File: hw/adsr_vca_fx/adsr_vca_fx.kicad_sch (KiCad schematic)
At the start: 0 parts

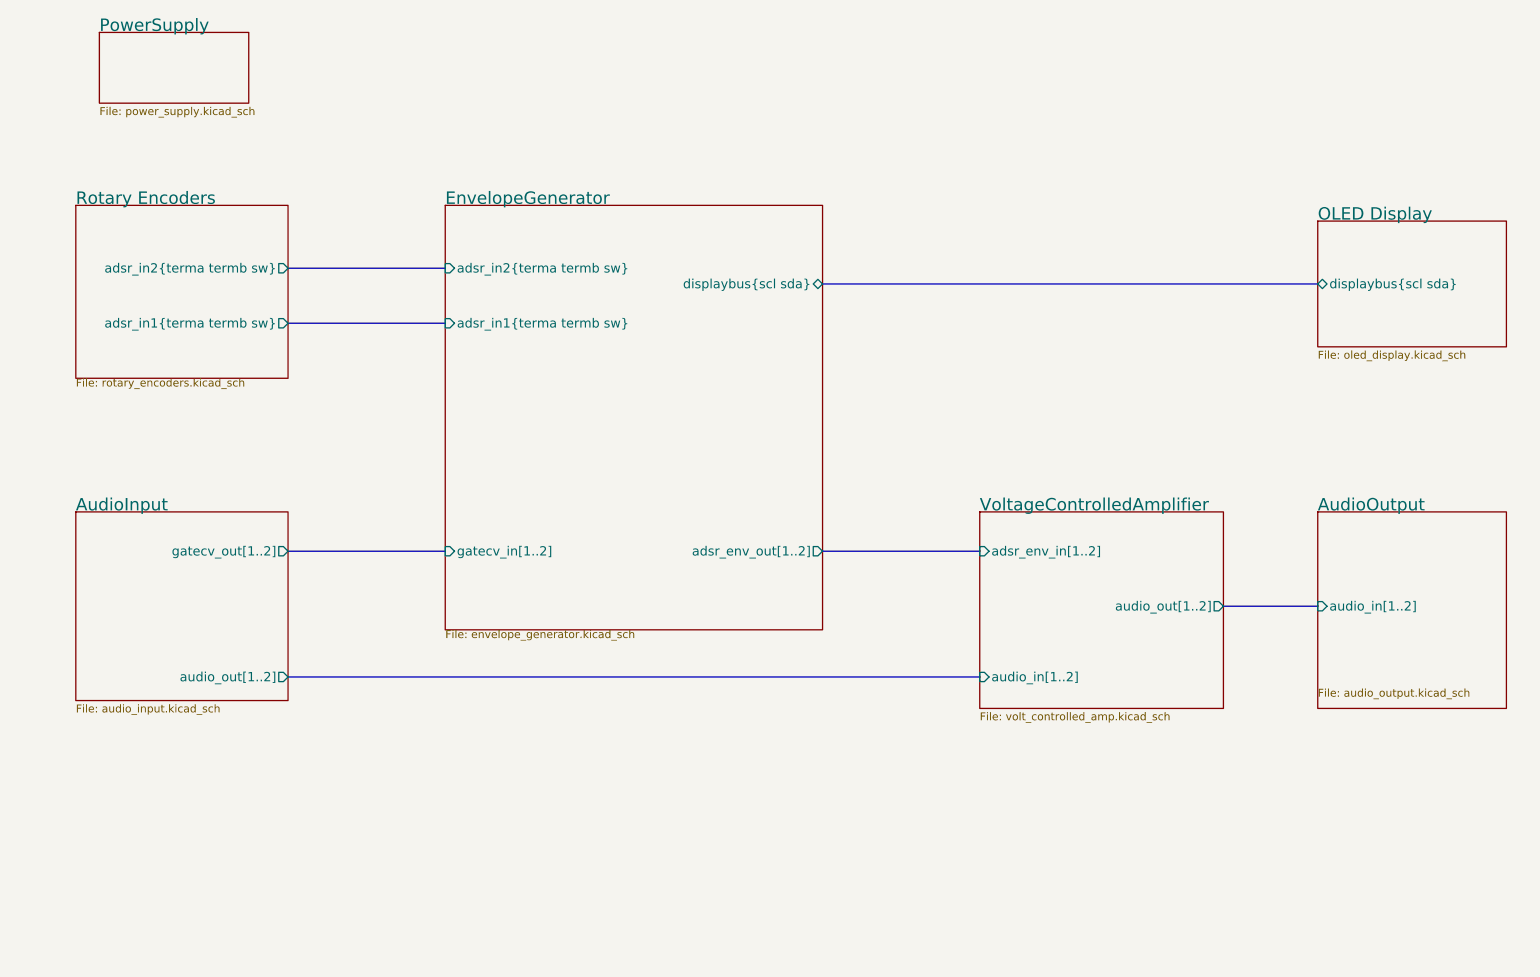
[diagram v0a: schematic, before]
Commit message: modified design into normal/inverted envlope
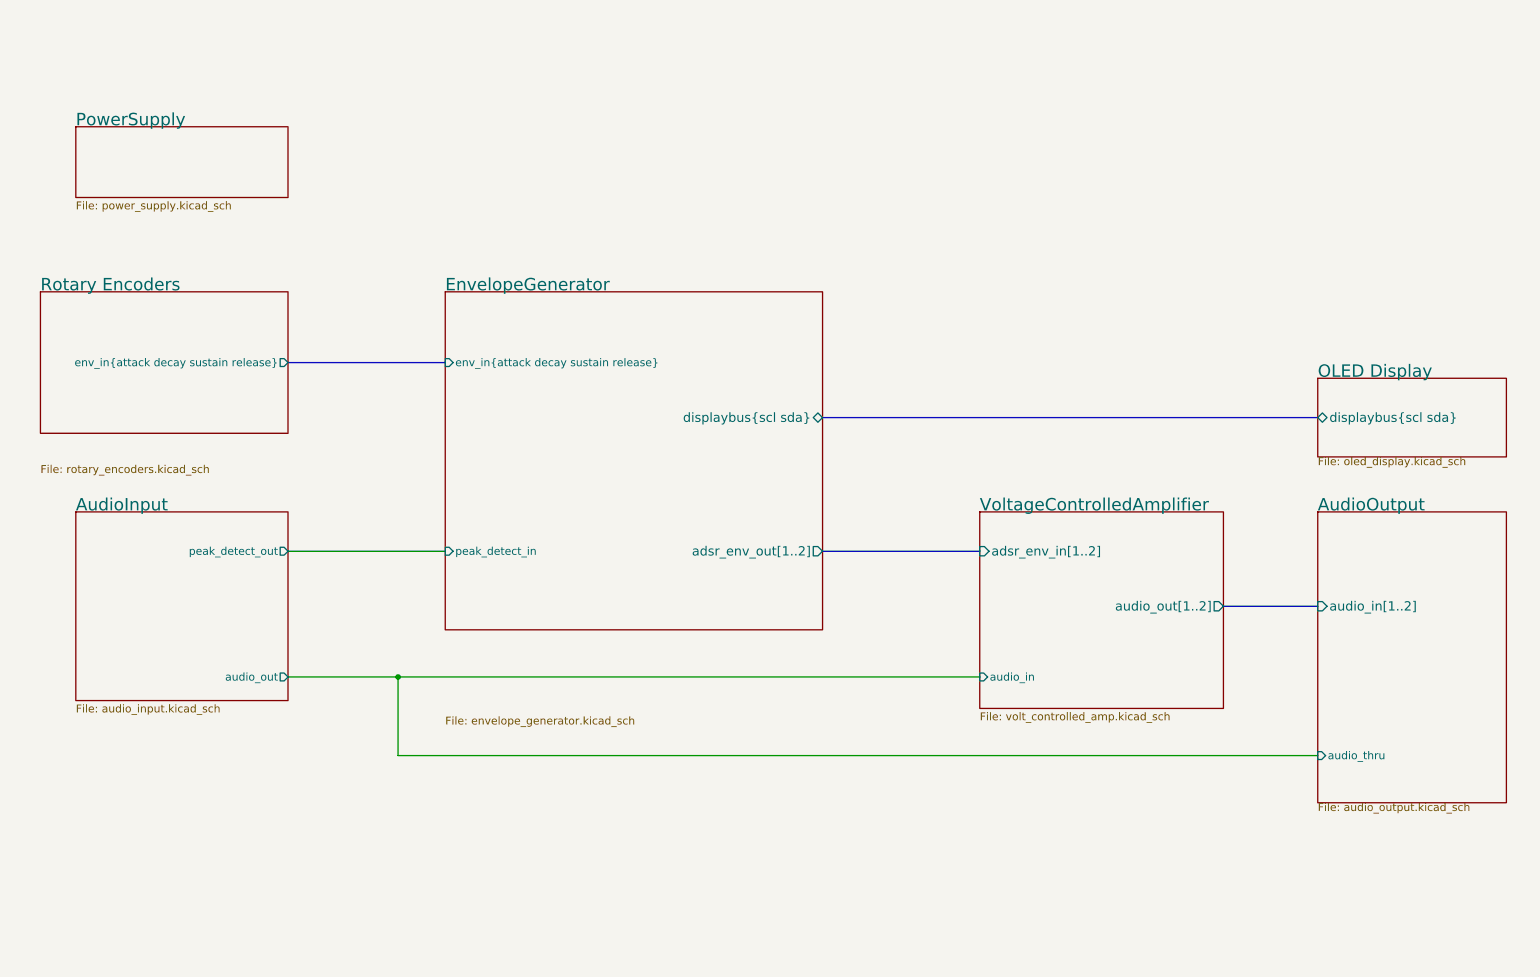
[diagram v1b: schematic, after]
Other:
- sheet AudioInput ports: added audio_out, peak_detect_out; removed audio_out[1..2], gatecv_out[1..2]
- sheet AudioOutput ports: added audio_thru; removed none
- sheet EnvelopeGenerator ports: added env_in{attack decay sustain release}, peak_detect_in; removed adsr_in1{terma termb sw}, adsr_in2{terma termb sw}, gatecv_in[1..2]
- sheet Rotary Encoders ports: added env_in{attack decay sustain release}; removed adsr_in1{terma termb sw}, adsr_in2{terma termb sw}
- sheet VoltageControlledAmplifier ports: added audio_in; removed audio_in[1..2]
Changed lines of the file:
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@@
 (kicad_sch (version 20230121) (generator eeschema)
   (paper "A4")
+  (junction (at 81.28 133.35) (diameter 0) (color 0 0 0 0)
+  )
   (bus (pts (xy 214.63 121.92) (xy 229.87 121.92))
+    (stroke (width 0) (type default))
+  )
+  (wire (pts (xy 81.28 133.35) (xy 63.5 133.35))
     (stroke (width 0) (type default))
   )
@@
     (stroke (width 0) (type default))
   )
-  (bus (pts (xy 63.5 76.2) (xy 88.9 76.2))
+  (bus (pts (xy 63.5 82.55) (xy 88.9 82.55))
     (stroke (width 0) (type default))
   )
-  (bus (pts (xy 63.5 67.31) (xy 88.9 67.31))
+  (wire (pts (xy 229.87 146.05) (xy 81.28 146.05))
     (stroke (width 0) (type default))
   )
-  (bus (pts (xy 63.5 113.03) (xy 88.9 113.03))
+  (wire (pts (xy 81.28 146.05) (xy 81.28 133.35))
     (stroke (width 0) (type default))
   )
-  (bus (pts (xy 63.5 133.35) (xy 175.26 133.35))
+  (wire (pts (xy 63.5 113.03) (xy 88.9 113.03))
     (stroke (width 0) (type default))
   )
-  (bus (pts (xy 149.86 69.85) (xy 229.87 69.85))
+  (wire (pts (xy 81.28 133.35) (xy 175.26 133.35))
+    (stroke (width 0) (type default))
+  )
+  (bus (pts (xy 149.86 91.44) (xy 229.87 91.44))
     (stroke (width 0) (type default))
   )
@@
       (effects (font (size 1.5 1.5)) (justify right))
     )
-    (pin "audio_in[1..2]" input (at 175.26 133.35 180)
+    (pin "adsr_env_in[1..2]" input (at 175.26 113.03 180)
       (effects (font (size 1.5 1.5)) (justify left))
     )
-    (pin "adsr_env_in[1..2]" input (at 175.26 113.03 180)
-      (effects (font (size 1.5 1.5)) (justify left))
+    (pin "audio_in" input (at 175.26 133.35 180)
+      (effects (font (size 1.27 1.27)) (justify left))
     )
     (instances
@@
       (effects (font (size 1.27 1.27)) (justify left top))
     )
-    (pin "audio_out[1..2]" output (at 63.5 133.35 0)
-      (effects (font (size 1.5 1.5)) (justify right))
+    (pin "audio_out" output (at 63.5 133.35 0)
+      (effects (font (size 1.27 1.27)) (justify right))
     )
-    (pin "gatecv_out[1..2]" output (at 63.5 113.03 0)
-      (effects (font (size 1.5 1.5)) (justify right))
+    (pin "peak_detect_out" output (at 63.5 113.03 0)
+      (effects (font (size 1.27 1.27)) (justify right))
     )
     (instances
@@
     )
   )
-  (sheet (at 229.87 59.69) (size 30.48 20.32)
+  (sheet (at 229.87 85.09) (size 30.48 12.7)
     (stroke (width 0.1524) (type solid))
     (fill (color 0 0 0 0.0000))
-    (property "Sheetname" "OLED Display" (at 229.87 59.69 0)
+    (property "Sheetname" "OLED Display" (at 229.87 85.09 0)
       (effects (font (size 2 2)) (justify left bottom))
     )
-    (property "Sheetfile" "oled_display.kicad_sch" (at 229.87 80.5946 0)
+    (property "Sheetfile" "oled_display.kicad_sch" (at 229.87 97.79 0)
       (effects (font (size 1.27 1.27)) (justify left top))
     )
-    (property "Field2" "" (at 229.87 59.69 0)
+    (property "Field2" "" (at 229.87 85.09 0)
       (effects (font (size 1.27 1.27)) hide)
     )
-    (pin "displaybus{scl sda}" bidirectional (at 229.87 69.85 180)
+    (pin "displaybus{scl sda}" bidirectional (at 229.87 91.44 180)
       (effects (font (size 1.5 1.5)) (justify left))
     )
@@
     )
   )
-  (sheet (at 88.9 57.15) (size 60.96 68.58)
+  (sheet (at 88.9 71.12) (size 60.96 54.61)
     (stroke (width 0.1524) (type solid))
     (fill (color 0 0 0 0.0000))
-    (property "Sheetname" "EnvelopeGenerator" (at 88.9 57.15 0)
+    (property "Sheetname" "EnvelopeGenerator" (at 88.9 71.12 0)
       (effects (font (size 2 2)) (justify left bottom))
     )
-    (property "Sheetfile" "envelope_generator.kicad_sch" (at 88.9 125.73 0)
+    (property "Sheetfile" "envelope_generator.kicad_sch" (at 88.9 139.7 0)
       (effects (font (size 1.27 1.27)) (justify left top))
     )
-    (pin "displaybus{scl sda}" bidirectional (at 149.86 69.85 0)
+    (pin "displaybus{scl sda}" bidirectional (at 149.86 91.44 0)
       (effects (font (size 1.5 1.5)) (justify right))
-    )
-    (pin "adsr_in2{terma termb sw}" input (at 88.9 67.31 180)
-      (effects (font (size 1.5 1.5)) (justify left))
-    )
-    (pin "adsr_in1{terma termb sw}" input (at 88.9 76.2 180)
-      (effects (font (size 1.5 1.5)) (justify left))
-    )
-    (pin "gatecv_in[1..2]" input (at 88.9 113.03 180)
-      (effects (font (size 1.5 1.5)) (justify left))
     )
     (pin "adsr_env_out[1..2]" output (at 149.86 113.03 0)
       (effects (font (size 1.5 1.5)) (justify right))
+    )
+    (pin "peak_detect_in" input (at 88.9 113.03 180)
+      (effects (font (size 1.27 1.27)) (justify left))
+    )
+    (pin "env_in{attack decay sustain release}" input (at 88.9 82.55 180)
+      (effects (font (size 1.27 1.27)) (justify left))
     )
     (instances
@@
     )
   )
-  (sheet (at 29.21 57.15) (size 34.29 27.94)
+  (sheet (at 23.495 71.12) (size 40.005 22.86)
     (stroke (width 0.1524) (type solid))
     (fill (color 0 0 0 0.0000))
-    (property "Sheetname" "Rotary Encoders" (at 29.21 57.15 0)
+    (property "Sheetname" "Rotary Encoders" (at 23.495 71.12 0)
       (effects (font (size 2 2)) (justify left bottom))
     )
-    (property "Sheetfile" "rotary_encoders.kicad_sch" (at 29.21 85.09 0)
+    (property "Sheetfile" "rotary_encoders.kicad_sch" (at 23.495 99.06 0)
       (effects (font (size 1.27 1.27)) (justify left top))
     )
-    (property "Field2" "" (at 29.21 57.15 0)
+    (property "Field2" "" (at 23.495 71.12 0)
       (effects (font (size 1.27 1.27)) hide)
     )
-    (pin "adsr_in2{terma termb sw}" output (at 63.5 67.31 0)
-      (effects (font (size 1.5 1.5)) (justify right))
-    )
-    (pin "adsr_in1{terma termb sw}" output (at 63.5 76.2 0)
-      (effects (font (size 1.5 1.5)) (justify right))
+    (pin "env_in{attack decay sustain release}" output (at 63.5 82.55 0)
+      (effects (font (size 1.27 1.27)) (justify right))
     )
     (instances
@@
     )
   )
-  (sheet (at 229.87 106.68) (size 30.48 31.75)
+  (sheet (at 229.87 106.68) (size 30.48 46.99)
     (stroke (width 0.1524) (type solid))
     (fill (color 0 0 0 0.0000))
@@
       (effects (font (size 2 2)) (justify left bottom))
     )
-    (property "Sheetfile" "audio_output.kicad_sch" (at 229.87 135.2046 0)
+    (property "Sheetfile" "audio_output.kicad_sch" (at 229.87 153.67 0)
       (effects (font (size 1.27 1.27)) (justify left top))
     )
     (pin "audio_in[1..2]" input (at 229.87 121.92 180)
       (effects (font (size 1.5 1.5)) (justify left))
+    )
+    (pin "audio_thru" input (at 229.87 146.05 180)
+      (effects (font (size 1.27 1.27)) (justify left))
     )
     (instances
@@
     )
   )
-  (sheet (at 33.02 29.21) (size 24.13 11.43)
+  (sheet (at 29.21 44.45) (size 34.29 11.43)
     (stroke (width 0.1524) (type solid))
     (fill (color 0 0 0 0.0000))
-    (property "Sheetname" "PowerSupply" (at 33.02 29.21 0)
+    (property "Sheetname" "PowerSupply" (at 29.21 44.45 0)
       (effects (font (size 2 2)) (justify left bottom))
     )
-    (property "Sheetfile" "power_supply.kicad_sch" (at 33.02 41.2246 0)
+    (property "Sheetfile" "power_supply.kicad_sch" (at 29.21 56.4646 0)
       (effects (font (size 1.27 1.27)) (justify left top))
     )

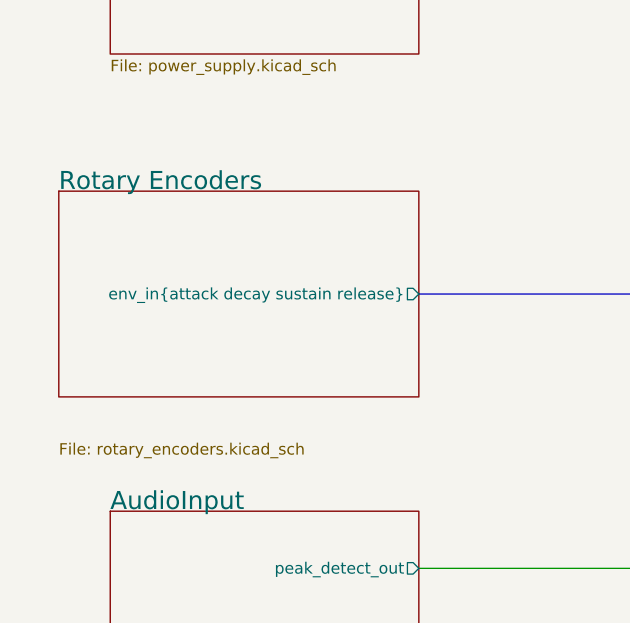
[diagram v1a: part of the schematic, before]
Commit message: renamed sheet
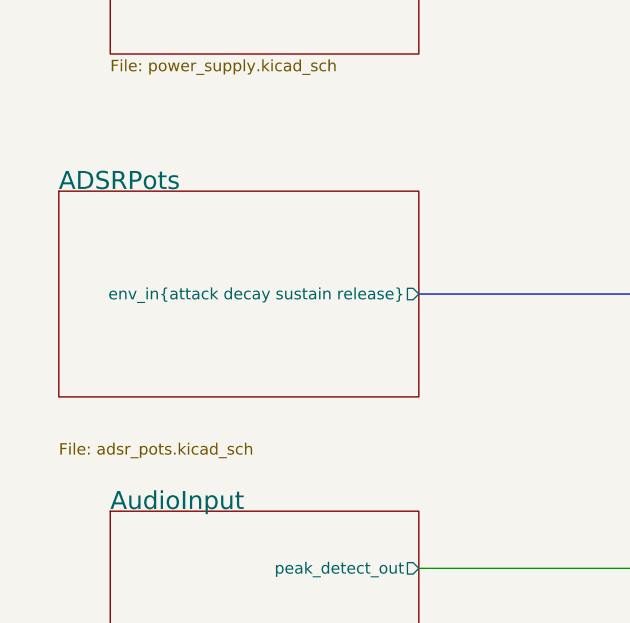
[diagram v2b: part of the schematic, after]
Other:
- sheet Rotary Encoders renamed ADSRPots
- sheet ADSRPots: file rotary_encoders.kicad_sch -> adsr_pots.kicad_sch
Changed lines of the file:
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@@
     (stroke (width 0.1524) (type solid))
     (fill (color 0 0 0 0.0000))
-    (property "Sheetname" "Rotary Encoders" (at 23.495 71.12 0)
+    (property "Sheetname" "ADSRPots" (at 23.495 71.12 0)
       (effects (font (size 2 2)) (justify left bottom))
     )
-    (property "Sheetfile" "rotary_encoders.kicad_sch" (at 23.495 99.06 0)
+    (property "Sheetfile" "adsr_pots.kicad_sch" (at 23.495 99.06 0)
       (effects (font (size 1.27 1.27)) (justify left top))
     )

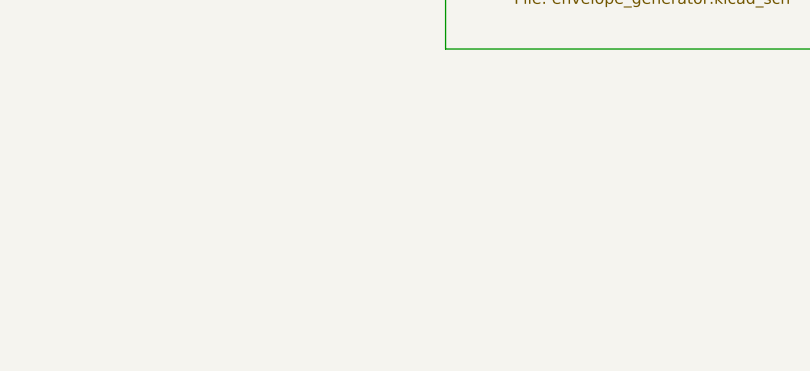
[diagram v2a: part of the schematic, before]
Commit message: updated layout
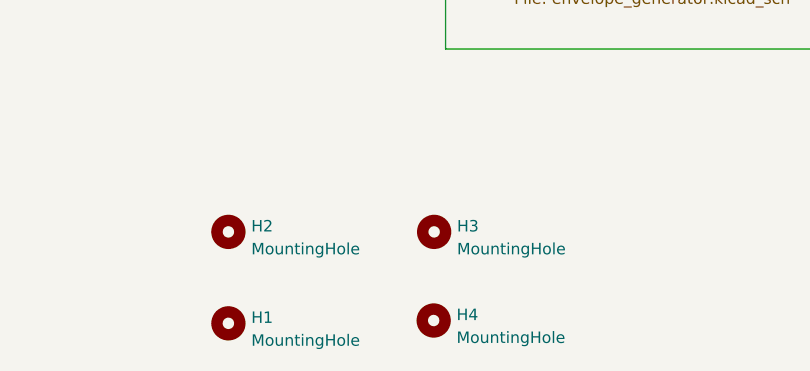
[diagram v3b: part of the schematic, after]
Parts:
- added H1, H2, H3, H4: MountingHole, MountingHole:MountingHole_3mm_Pad, symbol Mechanical:MountingHole
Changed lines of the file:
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@@
     (stroke (width 0) (type default))
+  )
+  (symbol (lib_id "Mechanical:MountingHole") (at 57.15 176.53 0) (unit 1)
+    (in_bom no) (on_board yes) (dnp no) (fields_autoplaced)
+    (property "Reference" "H1" (at 59.69 175.895 0)
+      (effects (font (size 1.27 1.27)) (justify left))
+    )
+    (property "Value" "MountingHole" (at 59.69 178.435 0)
+      (effects (font (size 1.27 1.27)) (justify left))
+    )
+    (property "Footprint" "MountingHole:MountingHole_3mm_Pad" (at 57.15 176.53 0)
+      (effects (font (size 1.27 1.27)) hide)
+    )
+    (property "Datasheet" "~" (at 57.15 176.53 0)
+      (effects (font (size 1.27 1.27)) hide)
+    )
+    (instances
+      (project "adsr_vca_fx"
+        (path "/2c7cc946-dcca-4ffb-b6a0-bf0c9ddb491b"
+          (reference "H1") (unit 1)
+        )
+      )
+    )
+  )
+  (symbol (lib_id "Mechanical:MountingHole") (at 57.15 166.37 0) (unit 1)
+    (in_bom no) (on_board yes) (dnp no) (fields_autoplaced)
+    (property "Reference" "H2" (at 59.69 165.735 0)
+      (effects (font (size 1.27 1.27)) (justify left))
+    )
+    (property "Value" "MountingHole" (at 59.69 168.275 0)
+      (effects (font (size 1.27 1.27)) (justify left))
+    )
+    (property "Footprint" "MountingHole:MountingHole_3mm_Pad" (at 57.15 166.37 0)
+      (effects (font (size 1.27 1.27)) hide)
+    )
+    (property "Datasheet" "~" (at 57.15 166.37 0)
+      (effects (font (size 1.27 1.27)) hide)
+    )
+    (instances
+      (project "adsr_vca_fx"
+        (path "/2c7cc946-dcca-4ffb-b6a0-bf0c9ddb491b"
+          (reference "H2") (unit 1)
+        )
+      )
+    )
+  )
+  (symbol (lib_id "Mechanical:MountingHole") (at 80.01 166.37 0) (unit 1)
+    (in_bom no) (on_board yes) (dnp no) (fields_autoplaced)
+    (property "Reference" "H3" (at 82.55 165.735 0)
+      (effects (font (size 1.27 1.27)) (justify left))
+    )
+    (property "Value" "MountingHole" (at 82.55 168.275 0)
+      (effects (font (size 1.27 1.27)) (justify left))
+    )
+    (property "Footprint" "MountingHole:MountingHole_3mm_Pad" (at 80.01 166.37 0)
+      (effects (font (size 1.27 1.27)) hide)
+    )
+    (property "Datasheet" "~" (at 80.01 166.37 0)
+      (effects (font (size 1.27 1.27)) hide)
+    )
+    (instances
+      (project "adsr_vca_fx"
+        (path "/2c7cc946-dcca-4ffb-b6a0-bf0c9ddb491b"
+          (reference "H3") (unit 1)
+        )
+      )
+    )
+  )
+  (symbol (lib_id "Mechanical:MountingHole") (at 79.9585 176.2167 0) (unit 1)
+    (in_bom no) (on_board yes) (dnp no) (fields_autoplaced)
+    (property "Reference" "H4" (at 82.4985 175.5817 0)
+      (effects (font (size 1.27 1.27)) (justify left))
+    )
+    (property "Value" "MountingHole" (at 82.4985 178.1217 0)
+      (effects (font (size 1.27 1.27)) (justify left))
+    )
+    (property "Footprint" "MountingHole:MountingHole_3mm_Pad" (at 79.9585 176.2167 0)
+      (effects (font (size 1.27 1.27)) hide)
+    )
+    (property "Datasheet" "~" (at 79.9585 176.2167 0)
+      (effects (font (size 1.27 1.27)) hide)
+    )
+    (instances
+      (project "adsr_vca_fx"
+        (path "/2c7cc946-dcca-4ffb-b6a0-bf0c9ddb491b"
+          (reference "H4") (unit 1)
+        )
+      )
+    )
   )
   (sheet (at 175.26 106.68) (size 39.37 31.75)
